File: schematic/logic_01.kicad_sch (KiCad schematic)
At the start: 4 parts, among them U401 74HC14, U402 74HC14, U403 74HC14, U404 74HC04

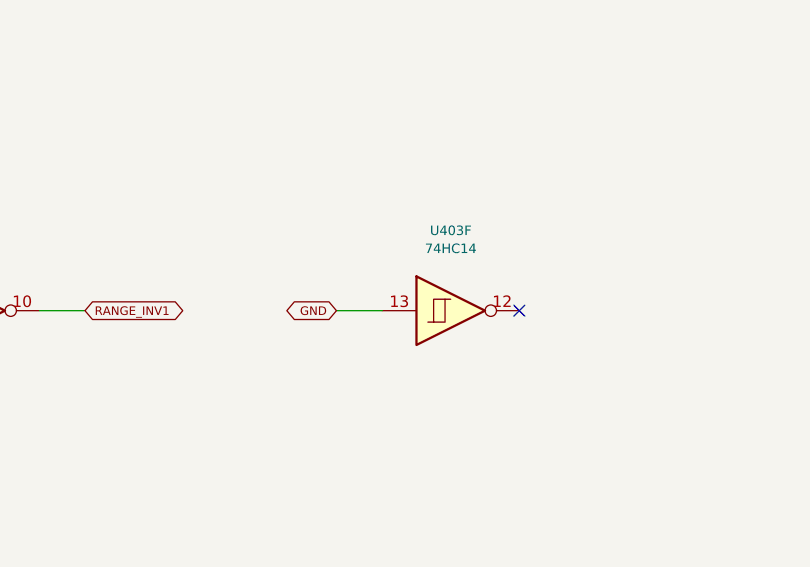
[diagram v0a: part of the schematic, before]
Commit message: add power supply, rail checks and parts list
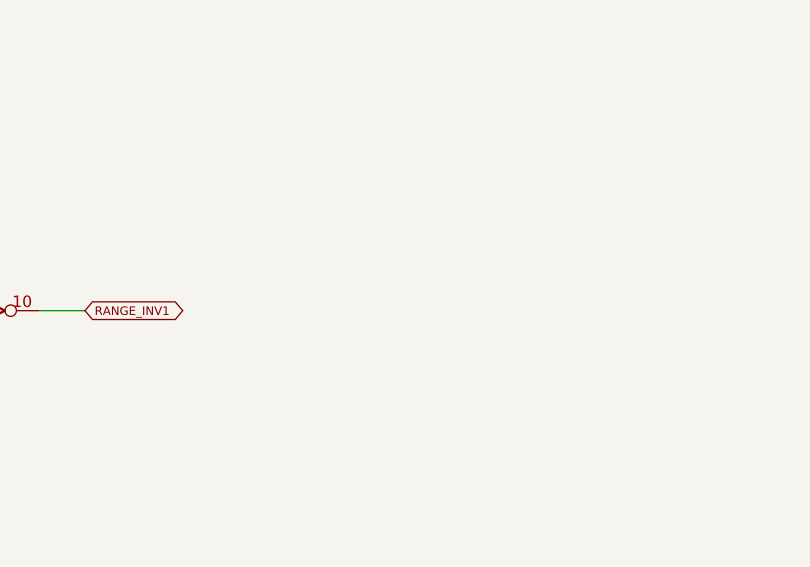
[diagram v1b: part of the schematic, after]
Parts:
- removed unit 6 of U403
- U401, U402, U403: MPN (none) -> 74HC14D,653; Manufacturer (none) -> Nexperia; Supplier (none) -> LCSC
- U404: MPN (none) -> 74HC04D,653; Manufacturer (none) -> Nexperia; Supplier (none) -> LCSC
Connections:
- no-connect marks 1 -> 0
